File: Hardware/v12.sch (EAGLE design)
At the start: 85 parts, among them J1 22-27-2081-08, J2 22-27-2031-03

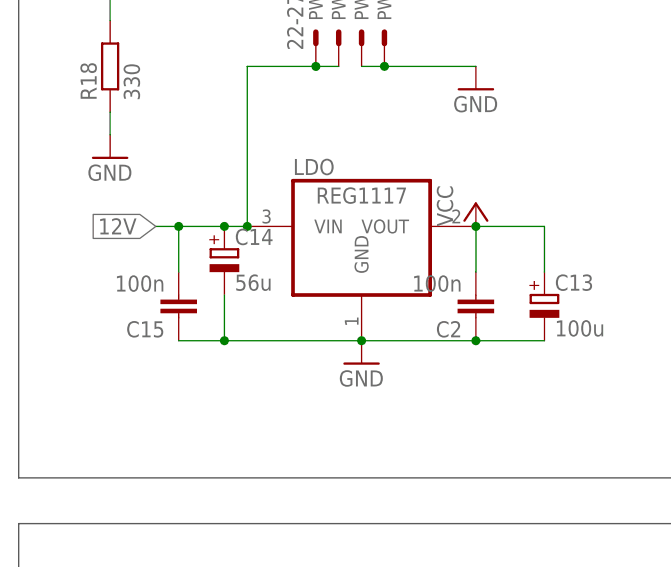
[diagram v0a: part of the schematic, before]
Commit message: Slight changes to correct values  of some capacitors.
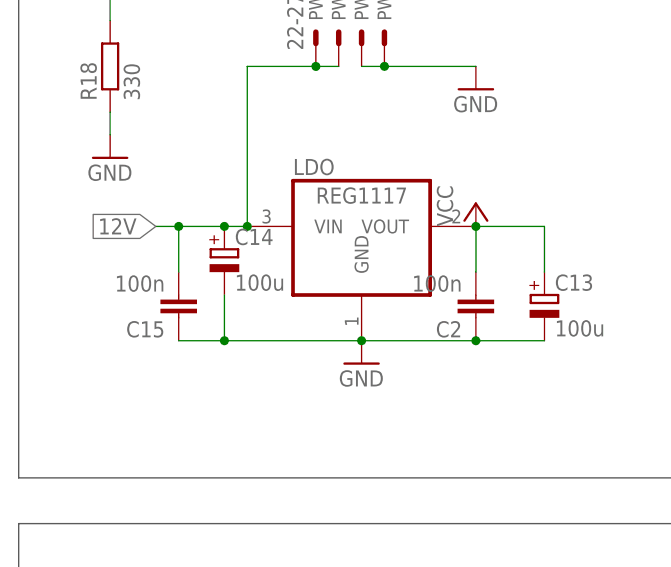
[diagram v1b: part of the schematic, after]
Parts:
- C14: value 56u -> 100u
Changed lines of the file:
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@@
 <part name="C15" library="rcl" deviceset="C-EU" device="C0603" value="100n"/>
 <part name="PWR_INPUT" library="con-molex" deviceset="22-?-04" device="27-2041"/>
-<part name="C14" library="rcl" deviceset="CPOL-EU" device="E2-5" value="56u"/>
+<part name="C14" library="rcl" deviceset="CPOL-EU" device="E2-5" value="100u"/>
 <part name="C10" library="rcl" deviceset="C-EU" device="C0603" value="10n"/>
 <part name="GND17" library="supply1" deviceset="GND" device=""/>
